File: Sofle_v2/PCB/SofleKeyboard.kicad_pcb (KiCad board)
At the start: 2 copper layers, 143.5 x 115.5 mm, 89 parts, among them J1 LED, J2 4PIN, J3 OLED, SW1 SW_PUSH, SW10 SW_PUSH, SW11 SW_PUSH, SW12 SW_PUSH, SW13 SW_PUSH, SW14 SW_PUSH, SW15 SW_PUSH, SW16 SW_PUSH, SW17 SW_PUSH, SW18 SW_PUSH, SW19 SW_PUSH, SW2 SW_PUSH, SW20 SW_PUSH, SW21 SW_PUSH, SW22 SW_PUSH, SW23 SW_PUSH, SW24 SW_PUSH, SW25 Rotary_Encoder_Switch, SW26 SW_PUSH, SW27 SW_PUSH, SW28 SW_PUSH, SW29 SW_PUSH, SW3 SW_PUSH, SW30 SW_PUSH, SW4 SW_PUSH, SW5 SW_PUSH, SW6 SW_PUSH, SW7 SW_PUSH, SW8 SW_PUSH, SW9 SW_PUSH, U1 ProMicro

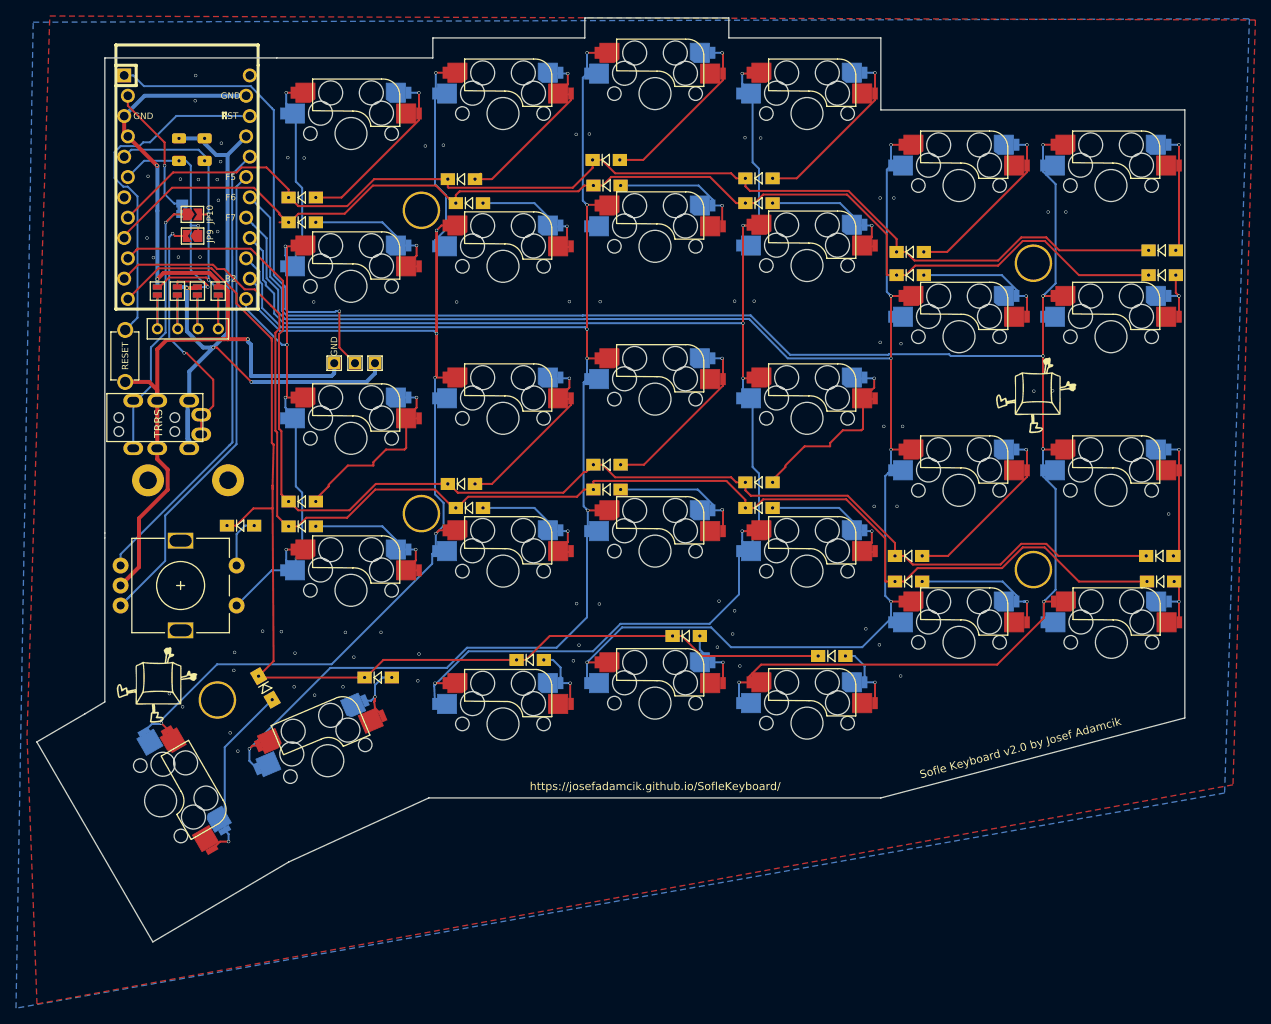
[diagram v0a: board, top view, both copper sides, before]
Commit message: First pass at comparison graphics Revised all keyboards to use outline stubbs Generated nested SVG's and color pallete
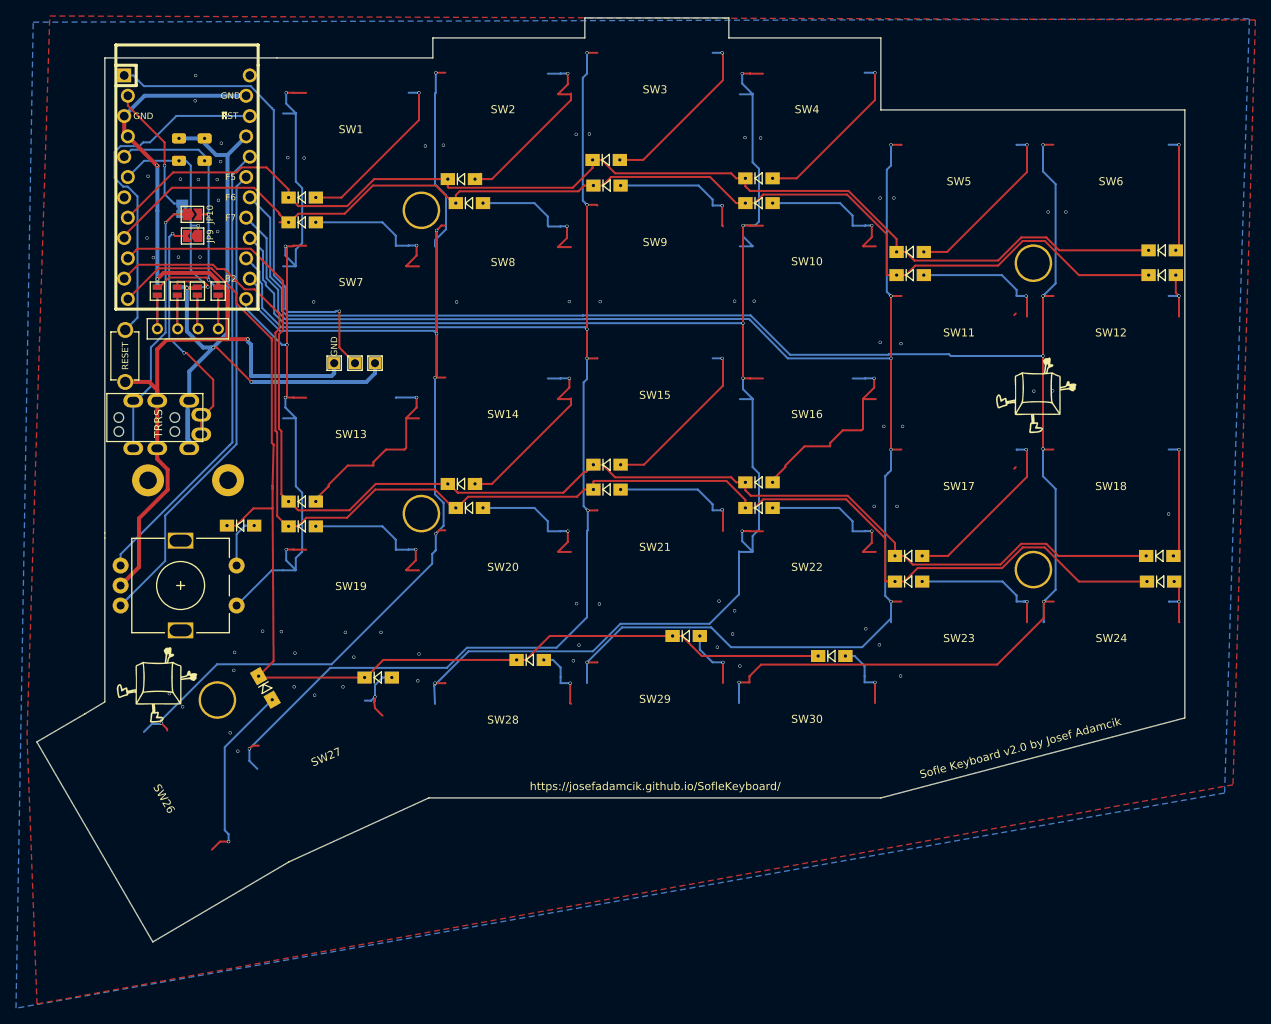
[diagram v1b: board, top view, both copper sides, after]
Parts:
- SW1, SW10, SW11, SW12, SW13, SW14, SW15, SW16, SW17, SW18, SW19, SW2, SW20, SW21, SW22, SW23, SW24, SW27, SW28, SW29, SW3, SW30, SW4, SW5, SW6, SW7, SW8, SW9: footprint SofleKeyboard-footprint:CherryMX_Hotswap -> ergodonk_kicad_library:key_outline_only
- SW26: footprint SofleKeyboard-footprint:CherryMX_Hotswap_1.5 -> ergodonk_kicad_library:key_outline_only
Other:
- net class Default removed
- net class GND removed
- net class VCC removed
